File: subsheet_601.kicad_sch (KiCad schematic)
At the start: 12 parts, among them U632 74LS244_PHY

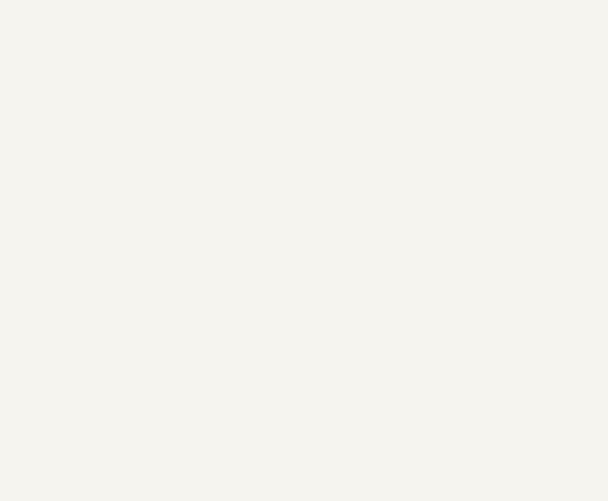
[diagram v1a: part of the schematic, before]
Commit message: add gnd/vcc symbol to start replacing local labels
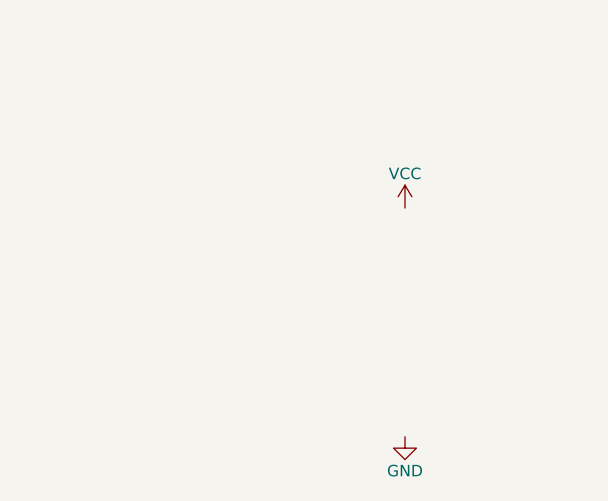
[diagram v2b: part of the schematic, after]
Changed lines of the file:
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@@
     (pin "8")
   )
+  (symbol (lib_id "power:VCC") (at 173.99 175.26 0) (unit 1)
+    (in_bom yes) (on_board yes)
+    (property "Reference" "#PWR?" (id 0) (at 173.99 179.07 0)
+      (effects (font (size 1.27 1.27)) hide)
+    )
+    (property "Value" "VCC" (id 1) (at 173.99 171.45 0))
+    (property "Footprint" "" (id 2) (at 173.99 175.26 0)
+      (effects (font (size 1.27 1.27)) hide)
+    )
+    (property "Datasheet" "" (id 3) (at 173.99 175.26 0)
+      (effects (font (size 1.27 1.27)) hide)
+    )
+    (pin "1")
+  )
+  (symbol (lib_id "power:GND") (at 173.99 200.66 0) (unit 1)
+    (in_bom yes) (on_board yes)
+    (property "Reference" "#PWR?" (id 0) (at 173.99 207.01 0)
+      (effects (font (size 1.27 1.27)) hide)
+    )
+    (property "Value" "GND" (id 1) (at 173.99 204.47 0))
+    (property "Footprint" "" (id 2) (at 173.99 200.66 0)
+      (effects (font (size 1.27 1.27)) hide)
+    )
+    (property "Datasheet" "" (id 3) (at 173.99 200.66 0)
+      (effects (font (size 1.27 1.27)) hide)
+    )
+    (pin "1")
+  )
 )
